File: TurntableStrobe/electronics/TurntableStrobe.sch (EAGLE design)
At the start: 15 parts, among them IC1 TINY25, J1 ISP, Q1 12MHz

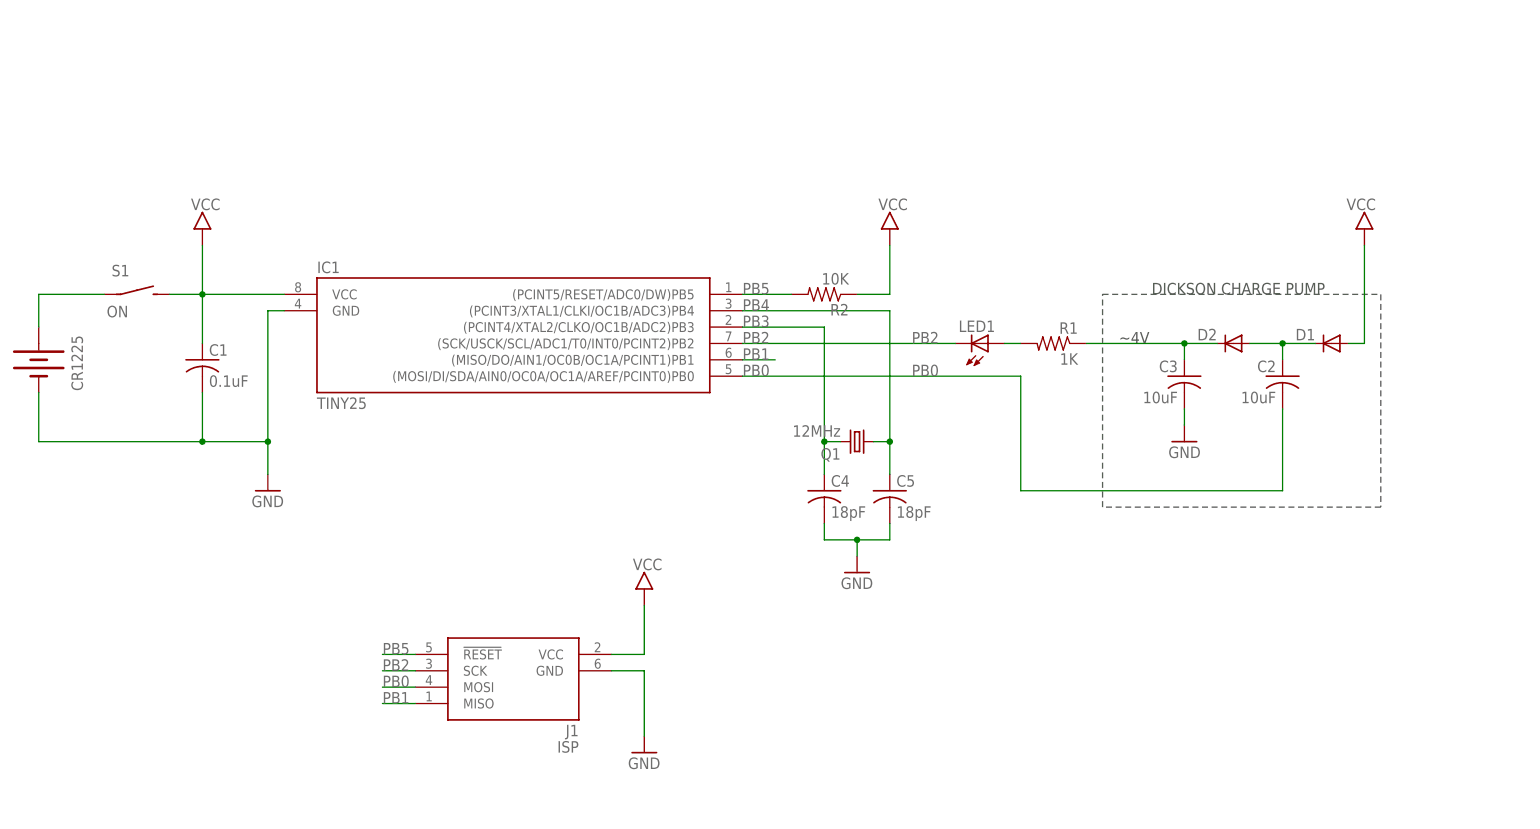
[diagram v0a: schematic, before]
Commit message: Fix for ISP (AVR910). Minor silk change.
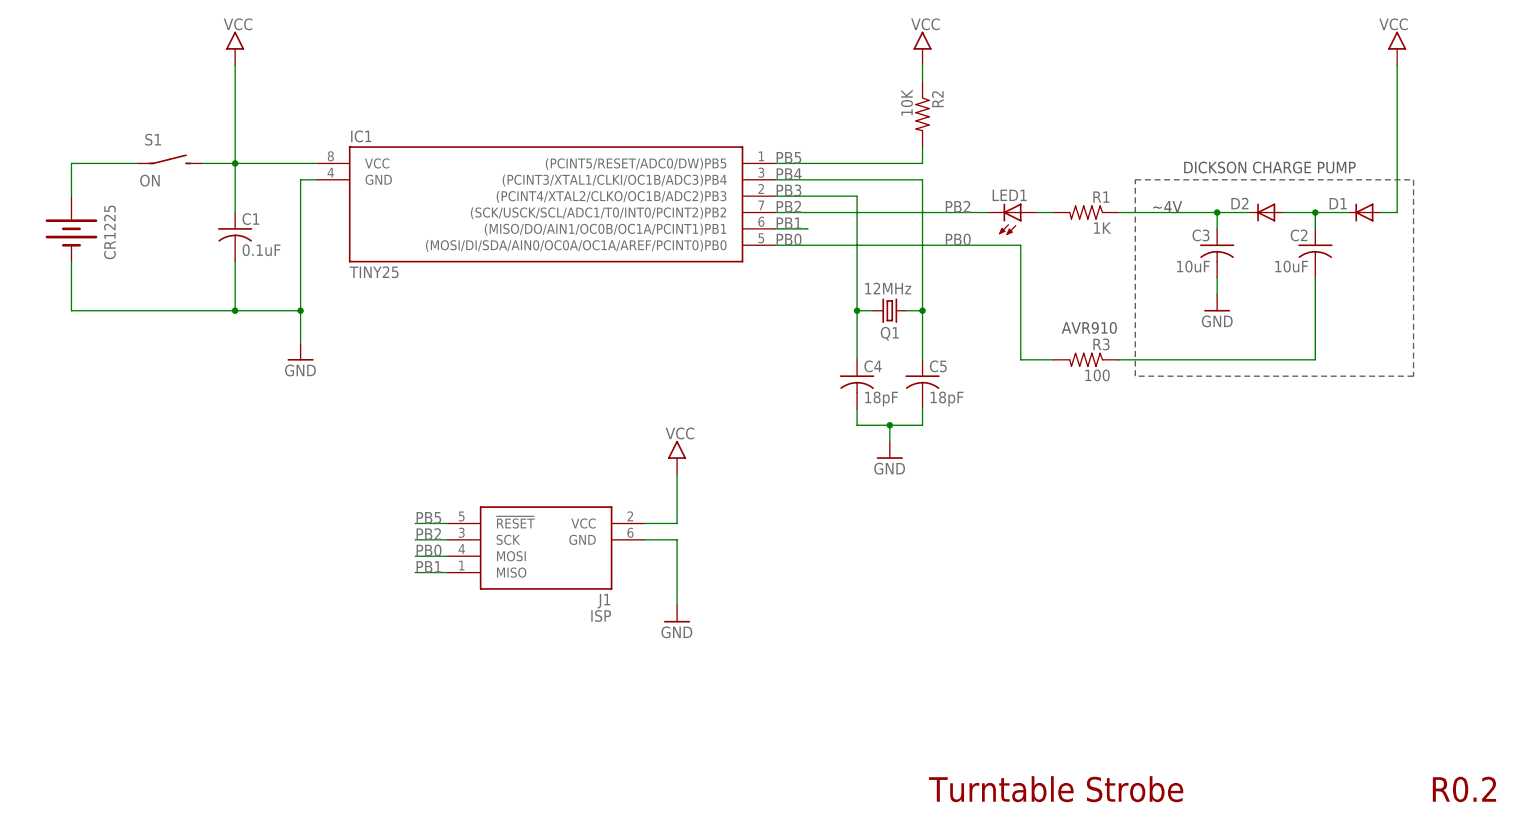
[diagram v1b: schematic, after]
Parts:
- added R3: 100, rcl:R-US_R0603
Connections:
- net N$1 renamed VBAT
- new net N$4: C2.2, R3.1
- net PB0: now also R3.2; no longer C2.2
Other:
- note added: "AVR910"
- note added: "R0.2"
- note added: "Turntable Strobe"
- moved on the sheet: C1, C2, C3, C4, C5, CR1225, D1, D2, IC1, J1, LED1, Q1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

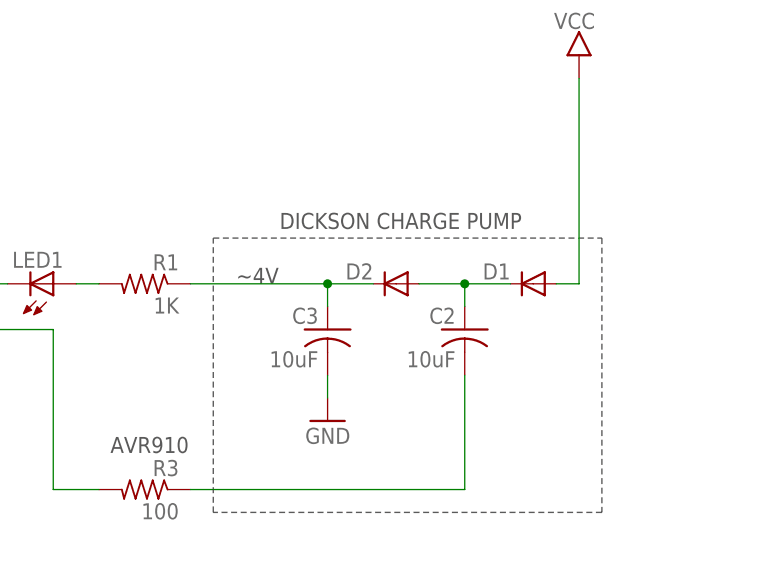
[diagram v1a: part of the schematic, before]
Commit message: Revise diode footprint
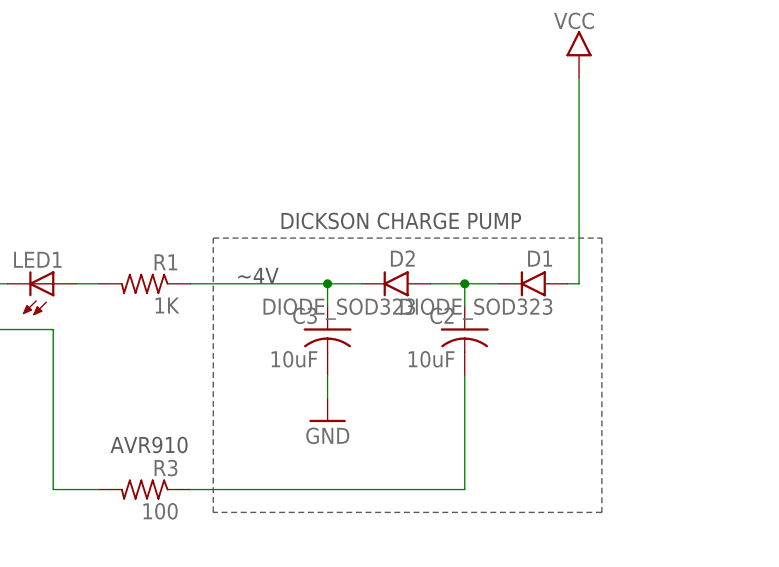
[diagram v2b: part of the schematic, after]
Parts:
- D1, D2: value (none) -> DIODE_SOD323; device SparkFun-DiscreteSemi:DIODESOD -> bt_diode:DIODE_SOD323
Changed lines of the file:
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@@
 <part name="C2" library="rcl" deviceset="C-US" device="C0603" value="10uF"/>
 <part name="C3" library="rcl" deviceset="C-US" device="C0603" value="10uF"/>
-<part name="D1" library="SparkFun-DiscreteSemi" deviceset="DIODE" device="SOD"/>
-<part name="D2" library="SparkFun-DiscreteSemi" deviceset="DIODE" device="SOD"/>
+<part name="D1" library="bt_diode" deviceset="DIODE" device="_SOD323"/>
+<part name="D2" library="bt_diode" deviceset="DIODE" device="_SOD323"/>
 <part name="GND4" library="mes" deviceset="GND" device=""/>
 <part name="U$4" library="mes" deviceset="VCC" device="" value=""/>
@@
 <instance part="C2" gate="G$1" x="198.12" y="55.88" rot="MR0"/>
 <instance part="C3" gate="G$1" x="182.88" y="55.88" rot="MR0"/>
-<instance part="D1" gate="G$1" x="205.74" y="60.96" rot="MR0"/>
-<instance part="D2" gate="G$1" x="190.5" y="60.96" rot="MR0"/>
+<instance part="D1" gate="D1" x="205.74" y="60.96" rot="MR0"/>
+<instance part="D2" gate="D1" x="190.5" y="60.96" rot="MR0"/>
 <instance part="GND4" gate="1" x="182.88" y="45.72" rot="MR0"/>
 <instance part="U$4" gate="G$1" x="210.82" y="83.82" rot="MR0"/>
@@
 </segment>
 <segment>
-<wire x1="208.28" y1="60.96" x2="210.82" y2="60.96" width="0.1524" layer="91"/>
+<wire x1="209.55" y1="60.96" x2="210.82" y2="60.96" width="0.1524" layer="91"/>
 <wire x1="210.82" y1="60.96" x2="210.82" y2="83.82" width="0.1524" layer="91"/>
 <pinref part="U$4" gate="G$1" pin="VCC"/>
-<pinref part="D1" gate="G$1" pin="A"/>
+<pinref part="D1" gate="D1" pin="A"/>
 </segment>
 </net>
@@
 <pinref part="C3" gate="G$1" pin="1"/>
 <wire x1="182.88" y1="58.42" x2="182.88" y2="60.96" width="0.1524" layer="91"/>
-<pinref part="D2" gate="G$1" pin="C"/>
-<wire x1="187.96" y1="60.96" x2="182.88" y2="60.96" width="0.1524" layer="91"/>
+<pinref part="D2" gate="D1" pin="C"/>
+<wire x1="186.69" y1="60.96" x2="182.88" y2="60.96" width="0.1524" layer="91"/>
 <pinref part="R1" gate="G$1" pin="1"/>
 <wire x1="182.88" y1="60.96" x2="167.64" y2="60.96" width="0.1524" layer="91"/>
@@
 <pinref part="C2" gate="G$1" pin="1"/>
 <wire x1="198.12" y1="58.42" x2="198.12" y2="60.96" width="0.1524" layer="91"/>
-<wire x1="198.12" y1="60.96" x2="203.2" y2="60.96" width="0.1524" layer="91"/>
-<pinref part="D1" gate="G$1" pin="C"/>
-<pinref part="D2" gate="G$1" pin="A"/>
-<wire x1="193.04" y1="60.96" x2="198.12" y2="60.96" width="0.1524" layer="91"/>
+<wire x1="198.12" y1="60.96" x2="201.93" y2="60.96" width="0.1524" layer="91"/>
+<pinref part="D1" gate="D1" pin="C"/>
+<pinref part="D2" gate="D1" pin="A"/>
+<wire x1="194.31" y1="60.96" x2="198.12" y2="60.96" width="0.1524" layer="91"/>
 <junction x="198.12" y="60.96"/>
 </segment>

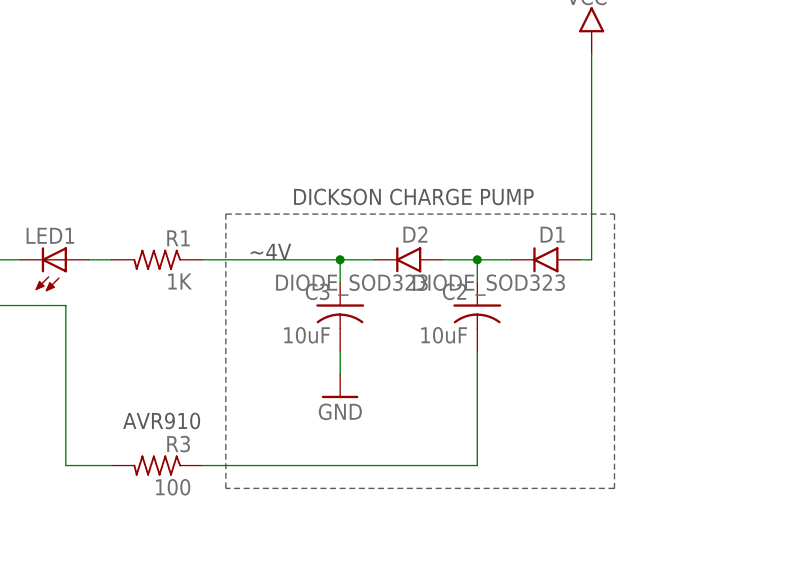
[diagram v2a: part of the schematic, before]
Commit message: Change diode value to specify 1N4148
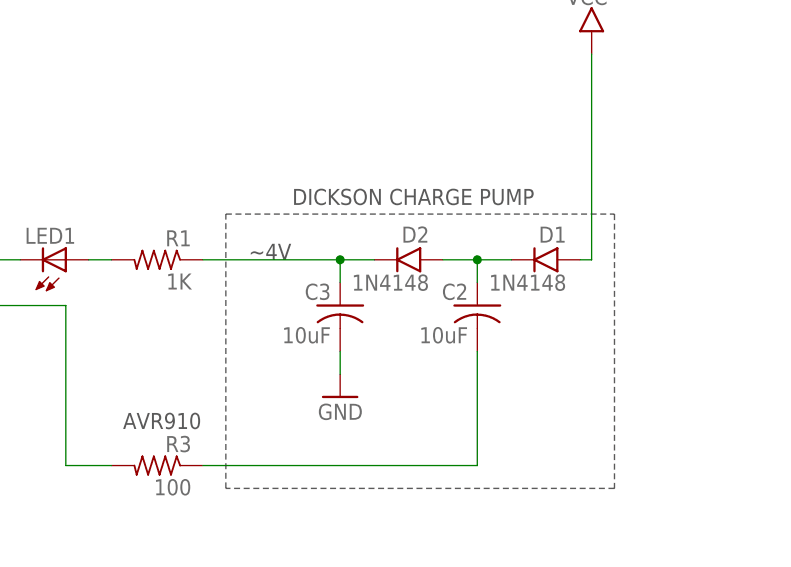
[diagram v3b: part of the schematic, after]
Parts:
- D1, D2: value DIODE_SOD323 -> 1N4148
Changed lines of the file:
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@@
 <part name="C2" library="rcl" deviceset="C-US" device="C0603" value="10uF"/>
 <part name="C3" library="rcl" deviceset="C-US" device="C0603" value="10uF"/>
-<part name="D1" library="bt_diode" deviceset="DIODE" device="_SOD323"/>
-<part name="D2" library="bt_diode" deviceset="DIODE" device="_SOD323"/>
+<part name="D1" library="bt_diode" deviceset="DIODE" device="_SOD323" value="1N4148"/>
+<part name="D2" library="bt_diode" deviceset="DIODE" device="_SOD323" value="1N4148"/>
 <part name="GND4" library="mes" deviceset="GND" device=""/>
 <part name="U$4" library="mes" deviceset="VCC" device="" value=""/>
